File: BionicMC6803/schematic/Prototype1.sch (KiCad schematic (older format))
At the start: 10 parts, among them SW1 TSD1265, U1 MC6803P, U2 74HCT541

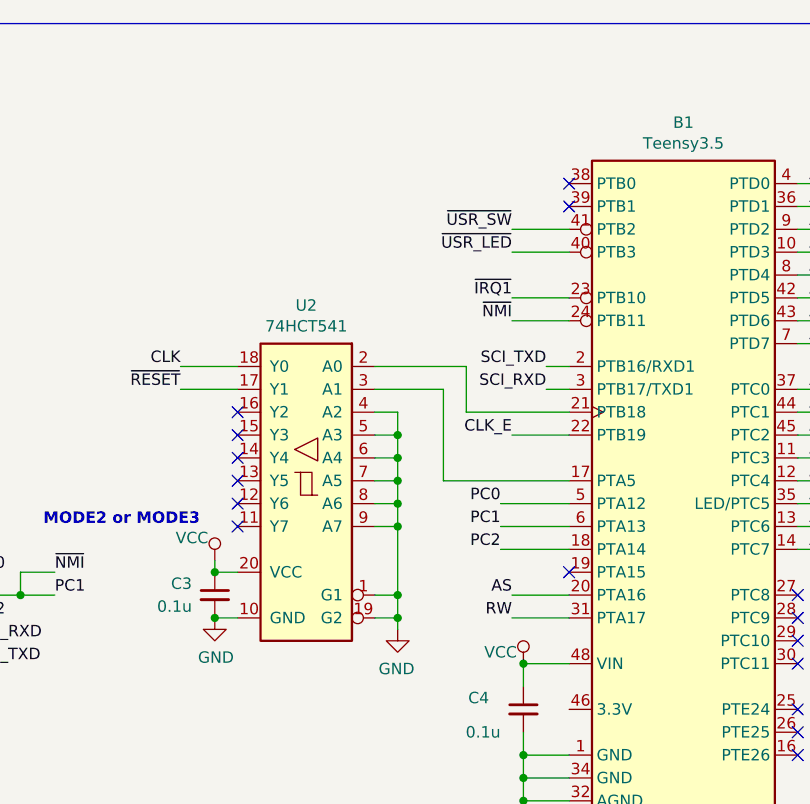
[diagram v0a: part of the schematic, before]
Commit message: [BionicMC6803] Update to BionicBase/Teensy35 configuration
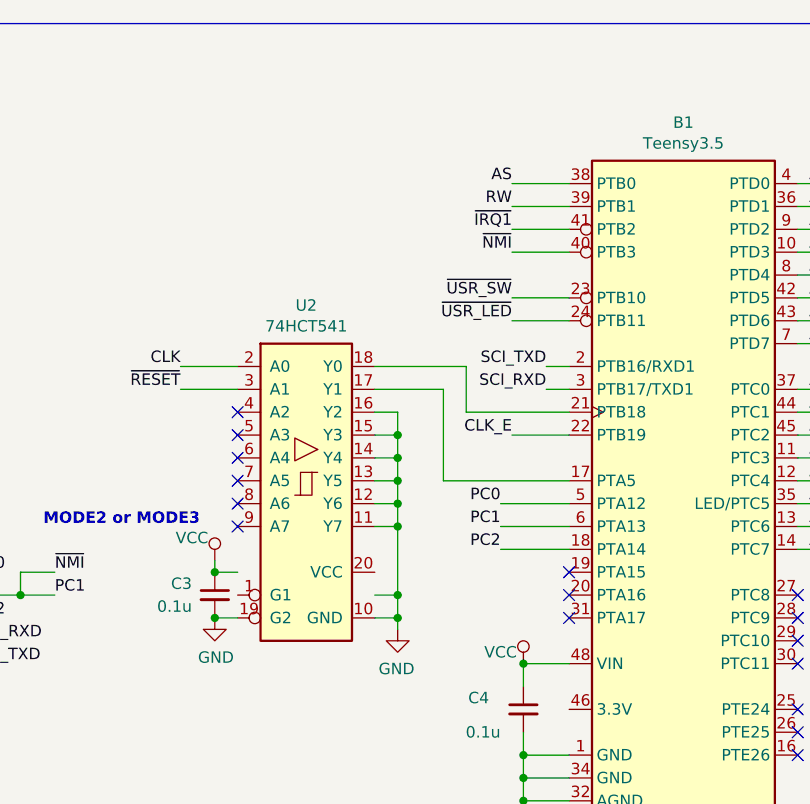
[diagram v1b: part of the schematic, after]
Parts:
- removed U2: 74HCT541, symbol 0-LocalLibrary:74HC541
- added U2: 74HCT541, symbol 0-LocalLibrary:74HCT541
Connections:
- net AS: now also B1.38 (PTB0); no longer B1.20 (PTA16)
- net CLK: now also U2.2 (A0)
- net GND: now also U2.10 (GND), U2.11 (Y7), U2.12 (Y6), U2.13 (Y5), U2.14 (Y4), U2.15 (Y3), U2.16 (Y2), U2.19 (G2)
- net PC1: now also B1.40 (PTB3); no longer B1.24 (PTB11)
- net RW: now also B1.39 (PTB1); no longer B1.31 (PTA17)
- net ~IRQ1~: now also B1.41 (PTB2); no longer B1.23 (PTB10)
- net ~RESET~: now also U2.3 (A1)
- net ~USR_LED~: now also B1.24 (PTB11); no longer B1.40 (PTB3)
- net ~USR_SW~: now also B1.23 (PTB10); no longer B1.41 (PTB2)
- net at B1.21 (PTB18): now also U2.18 (Y0)
- net at B1.17 (PTA5): now also U2.17 (Y1)
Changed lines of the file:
@@
 Text Label 1850 3600 2    50   ~ 0
 AS
-Text Label 5600 3900 2    50   ~ 0
+Text Label 5600 2100 2    50   ~ 0
 AS
-Text Label 5600 4000 2    50   ~ 0
+Text Label 5600 2200 2    50   ~ 0
 RW
 Wire Wire Line
@@
 Text Label 4150 3000 2    50   ~ 0
 ~RESET~
-$Comp
-L 0-LocalLibrary:74HC541 U2
-U 1 1 600523D8
-P 4700 3400
-F 0 "U2" H 4700 4167 50  0000 C CNN
-F 1 "74HCT541" H 4700 4076 50  0000 C CNN
-F 2 "" H 4700 3400 50  0001 C CNN
-F 3 "" H 4700 3400 50  0001 C CNN
-	1    4700 3400
-	-1   0    0    -1
-$EndComp
 $Comp
 L power:VCC #PWR06
@@
 PC2
 Wire Wire Line
-	5600 3900 5850 3900
-Wire Wire Line
-	5600 4000 5850 4000
+	5600 2100 5850 2100
+Wire Wire Line
+	5600 2200 5850 2200
 Wire Wire Line
 	1850 3200 2150 3200
@@
 Wire Wire Line
 	5550 3600 5850 3600
-Text Label 5600 2700 2    50   ~ 0
+Text Label 5600 2400 2    50   ~ 0
 ~NMI~
-Text Label 5600 2600 2    50   ~ 0
+Text Label 5600 2300 2    50   ~ 0
 ~IRQ1~
 NoConn ~ 2150 2100
@@
 NoConn ~ 2150 2700
 NoConn ~ 2150 2800
-NoConn ~ 5850 2100
-NoConn ~ 5850 2200
 Wire Bus Line
 	7100 1400 3300 1400
@@
 	1    0    0    -1
 $EndComp
-$Comp
-L 0-LocalLibrary:MC6803P U1
-U 1 1 616C56FE
-P 2600 3200
-F 0 "U1" H 2600 4567 50  0000 C CNN
-F 1 "MC6803P" H 2600 4476 50  0000 C CNN
-F 2 "Package_DIP:DIP-40_W15.24mm" H 2650 1850 50  0001 C CIN
-F 3 "" H 2600 3200 50  0001 C CNN
-	1    2600 3200
-	1    0    0    -1
-$EndComp
 Wire Wire Line
 	1950 4200 2150 4200
@@
 NoConn ~ 4400 3500
 NoConn ~ 4400 3600
-Text Label 5600 2300 2    50   ~ 0
+Text Label 5600 2600 2    50   ~ 0
 ~USR_SW~
-Text Label 5600 2400 2    50   ~ 0
+Text Label 5600 2700 2    50   ~ 0
 ~USR_LED~
 Wire Wire Line
@@
 $EndComp
 Connection ~ 4300 4000
+NoConn ~ 5850 3900
+NoConn ~ 5850 4000
 $Comp
 L 0-LocalLibrary:Teensy3.5 B1
-U 1 1 600CD57D
+U 1 1 61852AEA
 P 6350 3200
 F 0 "B1" H 6350 4567 50  0000 C CNN
@@
 	1    0    0    -1
 $EndComp
+$Comp
+L 0-LocalLibrary:74HCT541 U2
+U 1 1 61854006
+P 4700 3400
+F 0 "U2" H 4700 4167 50  0000 C CNN
+F 1 "74HCT541" H 4700 4076 50  0000 C CNN
+F 2 "" H 4700 3400 50  0001 C CNN
+F 3 "http://www.ti.com/lit/gpn/sn74HCT541" H 4700 3400 50  0001 C CNN
+	1    4700 3400
+	1    0    0    -1
+$EndComp
+$Comp
+L 0-LocalLibrary:MC6803P U1
+U 1 1 61855B73
+P 2600 3200
+F 0 "U1" H 2600 4567 50  0000 C CNN
+F 1 "MC6803P" H 2600 4476 50  0000 C CNN
+F 2 "Package_DIP:DIP-40_W15.24mm" H 2650 1850 50  0001 C CIN
+F 3 "" H 2600 3200 50  0001 C CNN
+	1    2600 3200
+	1    0    0    -1
+$EndComp

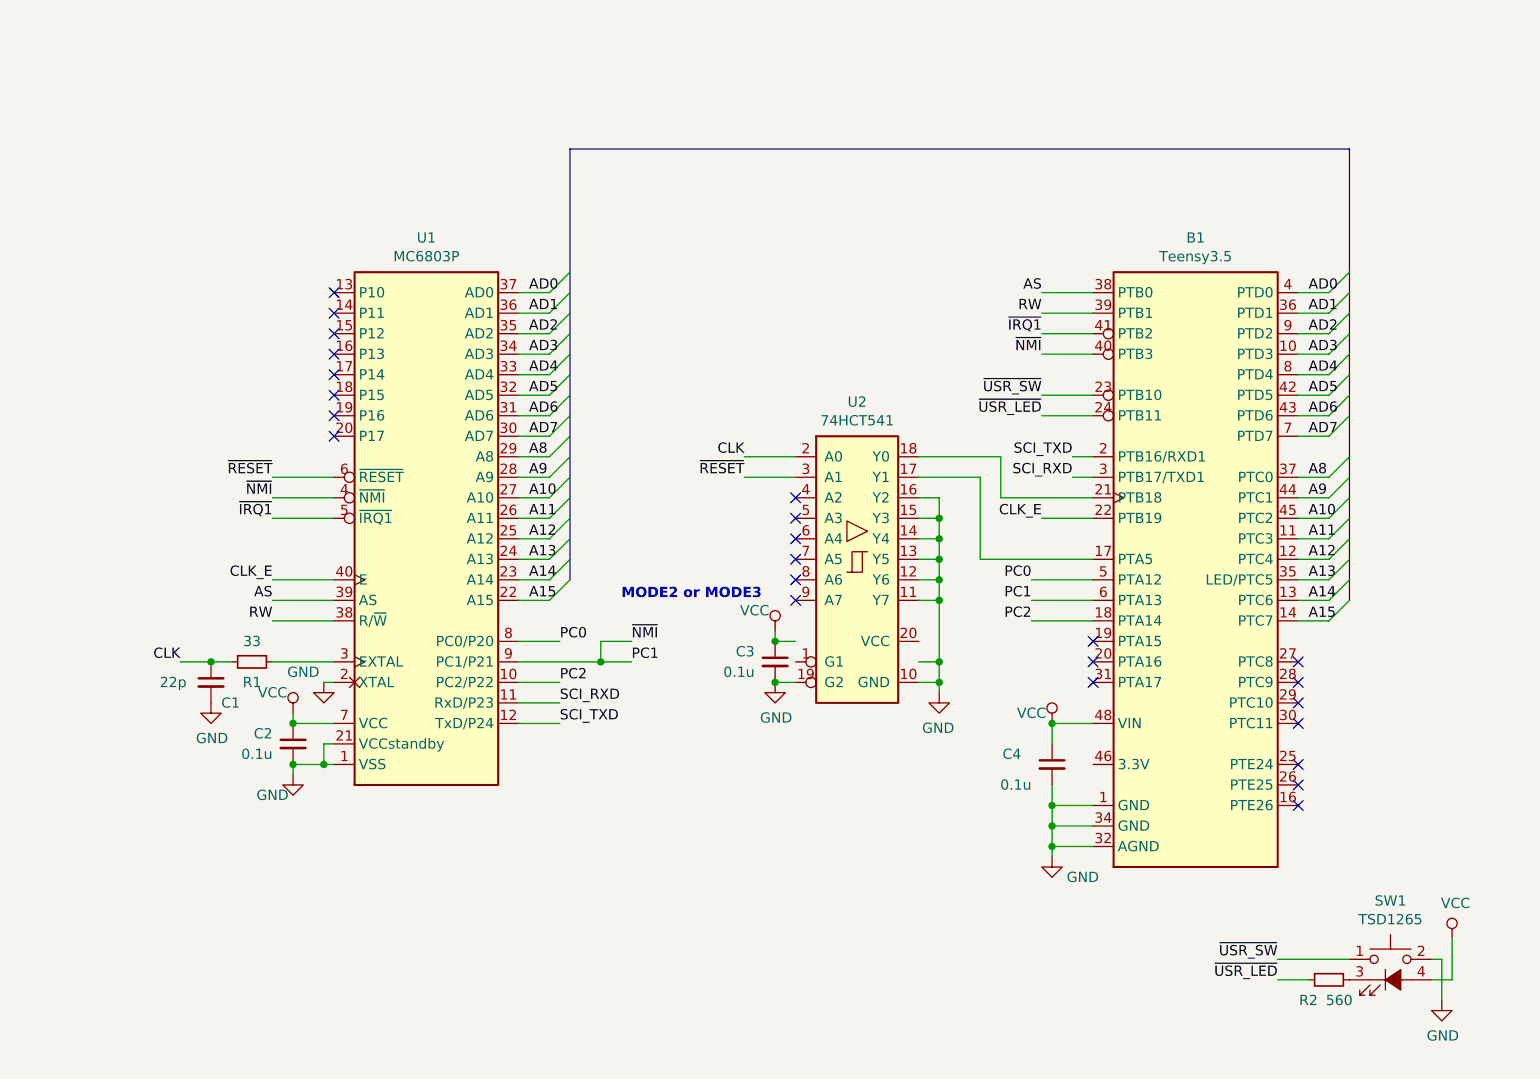
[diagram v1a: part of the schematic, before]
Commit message: [BionicMC6803] Mezzanine board
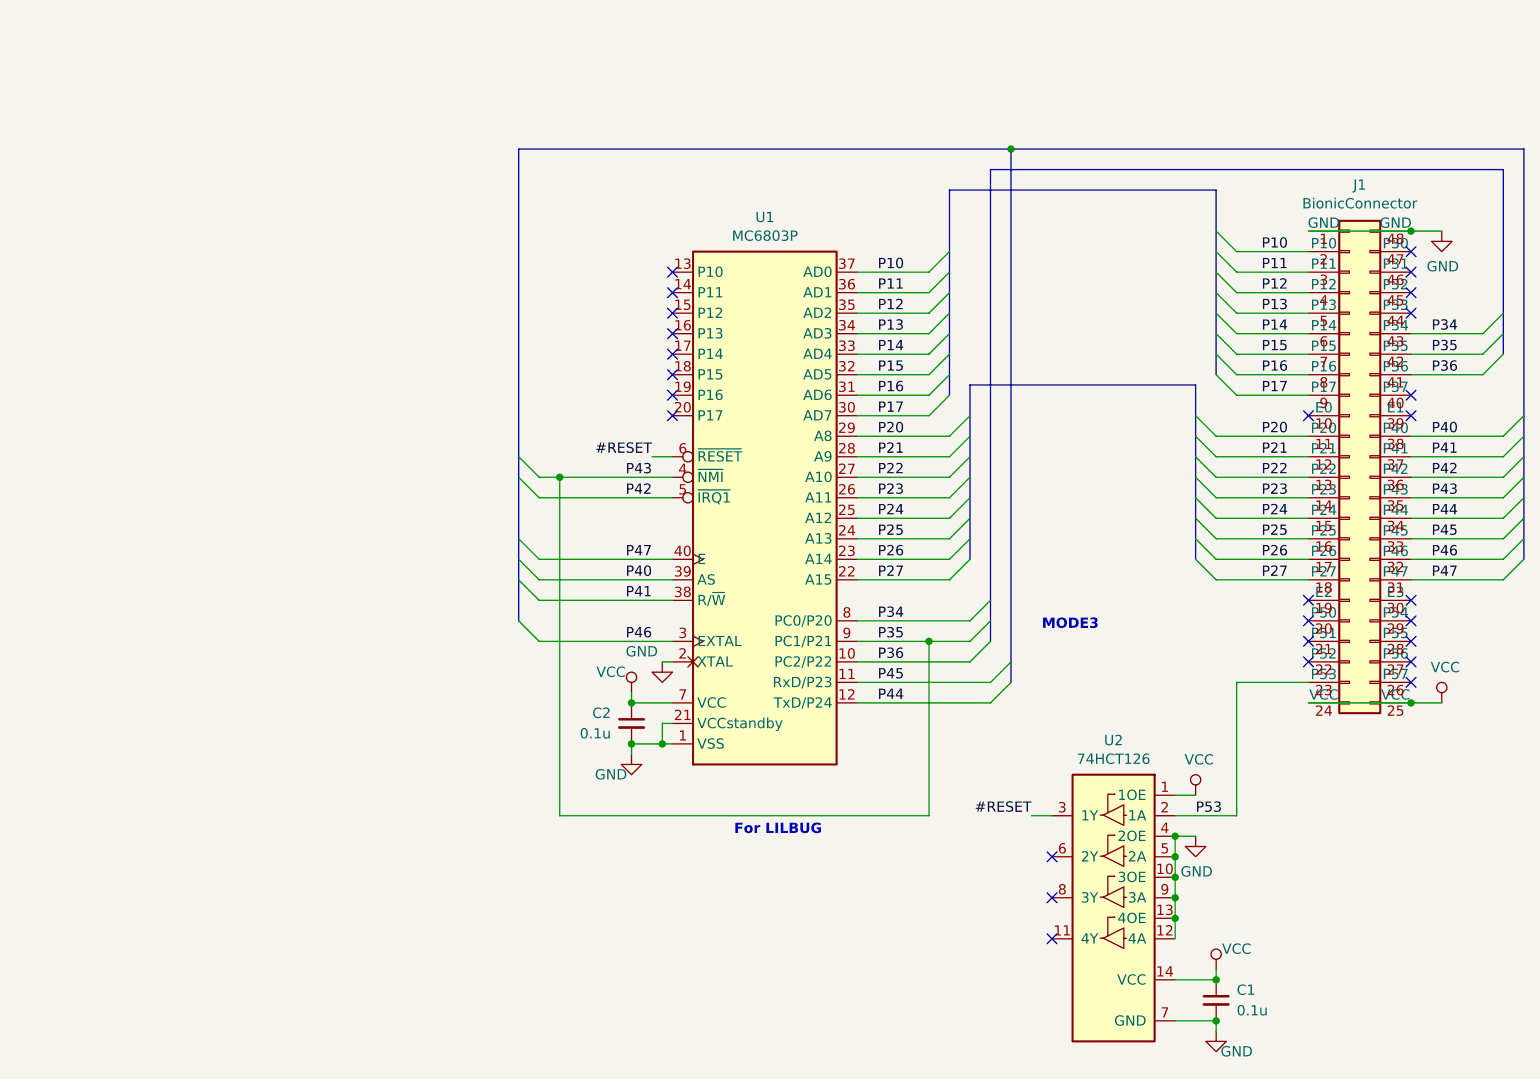
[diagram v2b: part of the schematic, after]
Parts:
- removed B1: Teensy3.5, Package_DIP:DIP-48_W15.24mm, symbol 0-LocalLibrary:Teensy3.5
- removed C3, C4: 0.1u, Capacitor_THT:C_Disc_D3.4mm_W2.1mm_P2.50mm, symbol Device:C_Small
- removed R1: 33, symbol Device:R_Small
- removed R2: 560, Resistor_THT:R_Axial_DIN0204_L3.6mm_D1.6mm_P5.08mm_Horizontal, symbol Device:R_Small
- removed SW1: TSD1265, 0-LocalLibrary:SW_PUSH-LED-12mm, symbol 0-LocalLibrary:SW_Push_LED
- removed U2: 74HCT541, symbol 0-LocalLibrary:74HCT541
- added J1: BionicConnector, 0-LocalLibrary:DIP-48_W10.16mm, symbol 0-LocalLibrary:BionicConnector
- added U2: 74HCT126, Package_DIP:DIP-14_W7.62mm, symbol 0-LocalLibrary:74HCT126
- C1: value 22p -> 0.1u; footprint (none) -> Capacitor_THT:C_Disc_D3.4mm_W2.1mm_P2.50mm
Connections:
- net CLK is gone; now on net VCC: C1.1
- net GND: now also J1.1 (GND), J1.48 (GND), U2.10 (3OE), U2.12 (4A), U2.13 (4OE), U2.4 (2OE), U2.5 (2A), U2.7 (GND), U2.9 (3A)
- net VCC: now also J1.24 (VCC), J1.25 (VCC), U2.1 (1OE), U2.14 (VCC)
- net P46: now reaches U1.3 (EXTAL)
- net P46: now also J1.32 (P46)
- net A10 renamed P22
- net P22: now also J1.13 (P22)
- net A11 renamed P23
- net P23: now also J1.14 (P23)
- net A12 renamed P24
- net P24: now also J1.15 (P24)
- net A13 renamed P25
- net P25: now also J1.16 (P25)
- net A14 renamed P26
- net P26: now also J1.17 (P26)
- net A15 renamed P27
- net P27: now also J1.18 (P27)
- net A8 renamed P20
- net P20: now also J1.11 (P20)
- net A9 renamed P21
- net P21: now also J1.12 (P21)
- net AD0 renamed P10
- net P10: now also J1.2 (P10)
- net AD1 renamed P11
- net P11: now also J1.3 (P11)
- net AD2 renamed P12
- net P12: now also J1.4 (P12)
- net AD3 renamed P13
- net P13: now also J1.5 (P13)
- net AD4 renamed P14
- net P14: now also J1.6 (P14)
- net AD5 renamed P15
- net P15: now also J1.7 (P15)
- net AD6 renamed P16
- net P16: now also J1.8 (P16)
- net AD7 renamed P17
- net P17: now also J1.9 (P17)
- net AS renamed P40
- net P40: now also J1.38 (P40)
- net CLK_E renamed P47
- net P47: now also J1.31 (P47)
- net PC0 renamed P34
- net P34: now also J1.43 (P34)
- net PC1 renamed P35
- net P35: now also J1.35 (P43), J1.42 (P35)
- net PC2 renamed P36
- net P36: now also J1.41 (P36)
- net RW renamed P41
- net P41: now also J1.37 (P41)
- net SCI_RXD renamed P45
- net P45: now also J1.33 (P45)
- net SCI_TXD renamed P44
- net P44: now also J1.34 (P44)
- net ~IRQ1~ renamed P42
- net P42: now also J1.36 (P42)
- net ~RESET~ renamed #RESET
- net #RESET: now also U2.3 (1Y)
- new net P53: J1.23 (P53), U2.2 (1A)
- no-connect marks 24 -> 27
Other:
- note added: "For LILBUG"
- note added: "MODE3"
- note removed: "MODE2 or MODE3"
- moved on the sheet: C2, U1
